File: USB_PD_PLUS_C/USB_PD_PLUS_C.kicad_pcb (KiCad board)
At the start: 4 copper layers, 54 x 45 mm, 57 parts, among them J1 USB3_A, Q2 FS8205A_C908265, U1 NDP1360KC, U10 NDP1360KC, U11 CXP0650-220M-AG(22UH), U12 TPS25740ARGER, U3 CH482D, U4 CXP0650-220M-AG(22UH), U5 LM317L_SOT-89

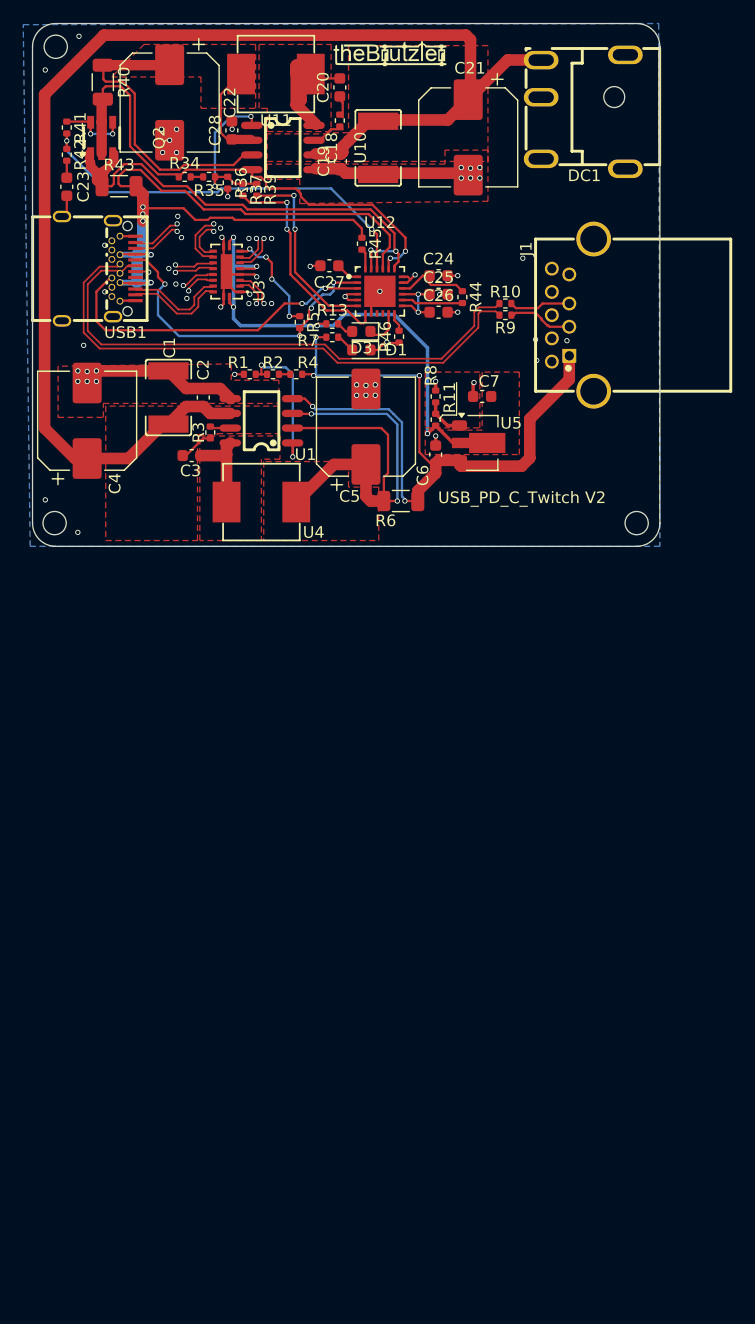
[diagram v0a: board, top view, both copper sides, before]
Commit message: Update Schematic to 3 Port USB-C Power
I updated the schamtic to 3 port usb-C with superspeed and PD working
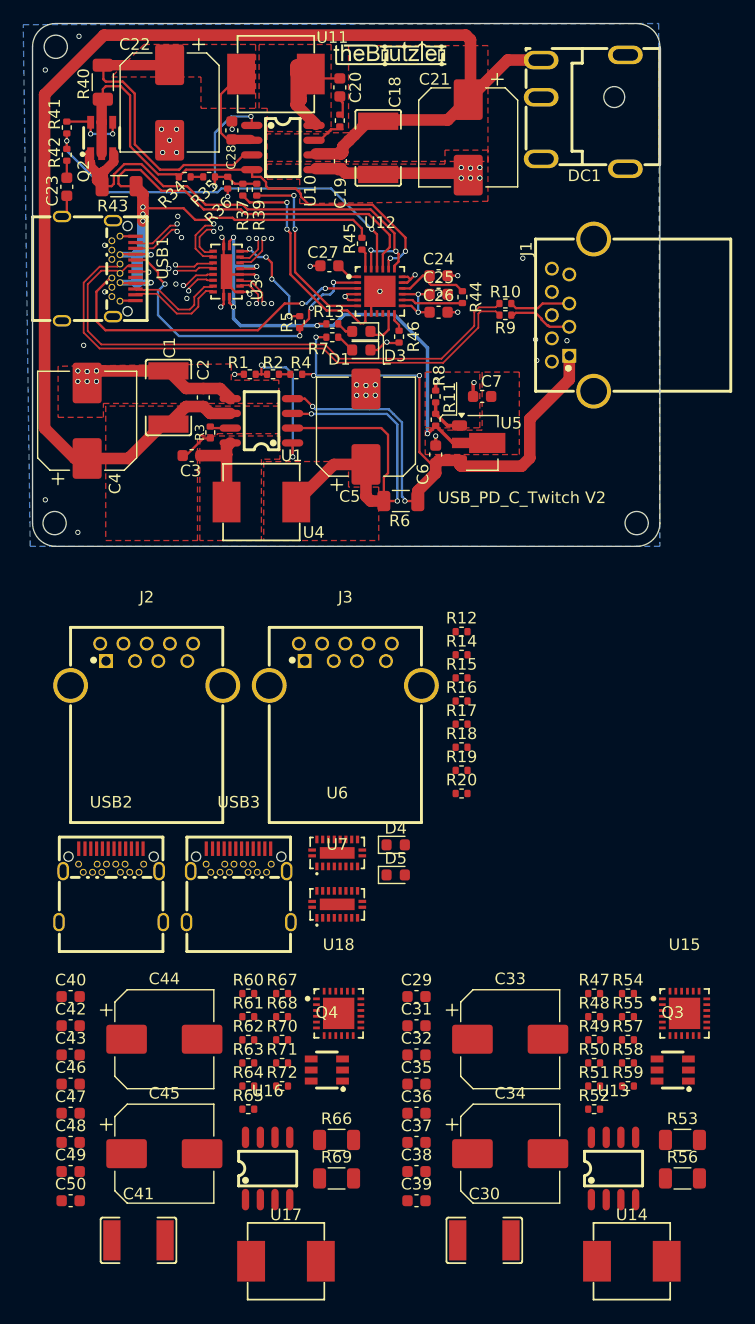
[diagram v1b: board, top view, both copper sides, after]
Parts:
- added C29: 100n, Capacitor_SMD:C_0603_1608Metric, F.Cu at (139.3, 104.7)
- added C30: 22u, easyeda2kicad:C1812, F.Cu at (145.2, 125.6)
- added C31: 100n, Capacitor_SMD:C_0603_1608Metric, F.Cu at (139.3, 107.2)
- added C32: 100n, Capacitor_SMD:C_0603_1608Metric, F.Cu at (139.3, 109.7)
- added C33: 100u, Capacitor_SMD:CP_Elec_8x10, F.Cu at (147.4, 108.3)
- added C34: 100u, Capacitor_SMD:CP_Elec_8x10, F.Cu at (147.4, 118.2)
- added C35: 100n, Capacitor_SMD:C_0603_1608Metric, F.Cu at (139.3, 112.2)
- added C36: 100n, Capacitor_SMD:C_0603_1608Metric, F.Cu at (139.3, 114.7)
- added C37: 100n, Capacitor_SMD:C_0603_1608Metric, F.Cu at (139.3, 117.2)
- added C38: 100n, Capacitor_SMD:C_0603_1608Metric, F.Cu at (139.3, 119.7)
- added C39: 100n, Capacitor_SMD:C_0603_1608Metric, F.Cu at (139.3, 122.2)
- added C40: 100n, Capacitor_SMD:C_0603_1608Metric, F.Cu at (109.6, 104.7)
- added C41: 22u, easyeda2kicad:C1812, F.Cu at (115.4, 125.6)
- added C42: 100n, Capacitor_SMD:C_0603_1608Metric, F.Cu at (109.6, 107.2)
- added C43: 100n, Capacitor_SMD:C_0603_1608Metric, F.Cu at (109.6, 109.7)
- added C44: 100u, Capacitor_SMD:CP_Elec_8x10, F.Cu at (117.6, 108.3)
- added C45: 100u, Capacitor_SMD:CP_Elec_8x10, F.Cu at (117.6, 118.2)
- added C46: 100n, Capacitor_SMD:C_0603_1608Metric, F.Cu at (109.6, 112.2)
- added C47: 100n, Capacitor_SMD:C_0603_1608Metric, F.Cu at (109.6, 114.7)
- added C48: 100n, Capacitor_SMD:C_0603_1608Metric, F.Cu at (109.6, 117.2)
- added C49: 100n, Capacitor_SMD:C_0603_1608Metric, F.Cu at (109.6, 119.7)
- added C50: 100n, Capacitor_SMD:C_0603_1608Metric, F.Cu at (109.6, 122.2)
- added D4: LED, LED_SMD:LED_0603_1608Metric, F.Cu at (137.6, 91.6)
- added D5: LED, LED_SMD:LED_0603_1608Metric, F.Cu at (137.6, 94.2)
- added J2: USB3_A, easyeda2kicad:USB-3.0-A-TH_HC-ST-003-01-Z, F.Cu at (116.1, 76.1)
- added J3: USB3_A, easyeda2kicad:USB-3.0-A-TH_HC-ST-003-01-Z, F.Cu at (133.2, 76.1)
- added Q3: FS8205A_C908265, easyeda2kicad:SOT-23-6_L2.9-W1.6-P0.95-LS2.8-BR, F.Cu at (161.4, 111.0)
- added Q4: FS8205A_C908265, easyeda2kicad:SOT-23-6_L2.9-W1.6-P0.95-LS2.8-BR, F.Cu at (131.6, 111.0)
- added R12: 0R, Resistor_SMD:R_0402_1005Metric, F.Cu at (143.2, 73.2)
- added R14: 10K, Resistor_SMD:R_0402_1005Metric, F.Cu at (143.2, 75.2)
- added R15: 0R, Resistor_SMD:R_0402_1005Metric, F.Cu at (143.2, 77.2)
- added R16: 10K, Resistor_SMD:R_0402_1005Metric, F.Cu at (143.2, 79.2)
- added R17: 22R, Resistor_SMD:R_0402_1005Metric, F.Cu at (143.2, 81.2)
- added R18: 22R, Resistor_SMD:R_0402_1005Metric, F.Cu at (143.2, 83.2)
- added R19: 22R, Resistor_SMD:R_0402_1005Metric, F.Cu at (143.2, 85.2)
- added R20: 22R, Resistor_SMD:R_0402_1005Metric, F.Cu at (143.2, 87.2)
- added R47: 100K, Resistor_SMD:R_0402_1005Metric, F.Cu at (154.6, 104.4)
- added R48: 8K, Resistor_SMD:R_0402_1005Metric, F.Cu at (154.6, 106.4)
- added R49: 25K, Resistor_SMD:R_0402_1005Metric, F.Cu at (154.6, 108.4)
- added R50: 29K, Resistor_SMD:R_0402_1005Metric, F.Cu at (154.6, 110.4)
- added R51: 22R, Resistor_SMD:R_0402_1005Metric, F.Cu at (154.6, 112.4)
- added R52: 18K, Resistor_SMD:R_0402_1005Metric, F.Cu at (154.6, 114.3)
- added R53: 10m, Resistor_SMD:R_1206_3216Metric, F.Cu at (162.2, 117.0)
- added R54: 10K, Resistor_SMD:R_0402_1005Metric, F.Cu at (157.6, 104.4)
- added R55: 10K, Resistor_SMD:R_0402_1005Metric, F.Cu at (157.6, 106.4)
- added R56: 6m, Resistor_SMD:R_1206_3216Metric, F.Cu at (162.2, 120.3)
- added R57: 100K, Resistor_SMD:R_0402_1005Metric, F.Cu at (157.6, 108.4)
- added R58: 100R, Resistor_SMD:R_0402_1005Metric, F.Cu at (157.6, 110.4)
- added R59: 100K, Resistor_SMD:R_0402_1005Metric, F.Cu at (157.6, 112.4)
- added R60: 100K, Resistor_SMD:R_0402_1005Metric, F.Cu at (124.9, 104.4)
- added R61: 8K, Resistor_SMD:R_0402_1005Metric, F.Cu at (124.9, 106.4)
- added R62: 25K, Resistor_SMD:R_0402_1005Metric, F.Cu at (124.9, 108.4)
- added R63: 29K, Resistor_SMD:R_0402_1005Metric, F.Cu at (124.9, 110.4)
- added R64: 22R, Resistor_SMD:R_0402_1005Metric, F.Cu at (124.9, 112.4)
- added R65: 18K, Resistor_SMD:R_0402_1005Metric, F.Cu at (124.9, 114.3)
- added R66: 10m, Resistor_SMD:R_1206_3216Metric, F.Cu at (132.5, 117.0)
- added R67: 10K, Resistor_SMD:R_0402_1005Metric, F.Cu at (127.8, 104.4)
- added R68: 10K, Resistor_SMD:R_0402_1005Metric, F.Cu at (127.8, 106.4)
- added R69: 6m, Resistor_SMD:R_1206_3216Metric, F.Cu at (132.5, 120.3)
- added R70: 100K, Resistor_SMD:R_0402_1005Metric, F.Cu at (127.8, 108.4)
- added R71: 100R, Resistor_SMD:R_0402_1005Metric, F.Cu at (127.8, 110.4)
- added R72: 100K, Resistor_SMD:R_0402_1005Metric, F.Cu at (127.8, 112.4)
- added U13: NDP1360KC, easyeda2kicad:SOP-8_L4.9-W3.9-P1.27-LS6.0-BL, F.Cu at (156.3, 119.5)
- added U14: CXP0650-220M-AG(22UH), easyeda2kicad:IND-SMD_L7.1-W6.6_CXP0650, F.Cu at (157.9, 127.4)
- added U15: TPS25740ARGER, easyeda2kicad:VQFN-24_L4.0-W4.0-P0.50-TL-EP, F.Cu at (162.4, 106.1)
- added U16: NDP1360KC, easyeda2kicad:SOP-8_L4.9-W3.9-P1.27-LS6.0-BL, F.Cu at (126.5, 119.5)
- added U17: CXP0650-220M-AG(22UH), easyeda2kicad:IND-SMD_L7.1-W6.6_CXP0650, F.Cu at (128.1, 127.4)
- added U18: TPS25740ARGER, easyeda2kicad:VQFN-24_L4.0-W4.0-P0.50-TL-EP, F.Cu at (132.7, 106.1)
- added U6: CH482D, easyeda2kicad:VFQFN-20_L4.5-W2.5-P0.5-BL-EP, F.Cu at (132.5, 92.3)
- added U7: CH482D, easyeda2kicad:VFQFN-20_L4.5-W2.5-P0.5-BL-EP, F.Cu at (132.5, 96.7)
- added USB2: HX TYPE-C 24P QCHT, easyeda2kicad:TYPE-C-SMD_TYPE-C-24P-QCHT, F.Cu at (113.1, 95.1)
- added USB3: HX TYPE-C 24P QCHT, easyeda2kicad:TYPE-C-SMD_TYPE-C-24P-QCHT, F.Cu at (124.0, 95.1)

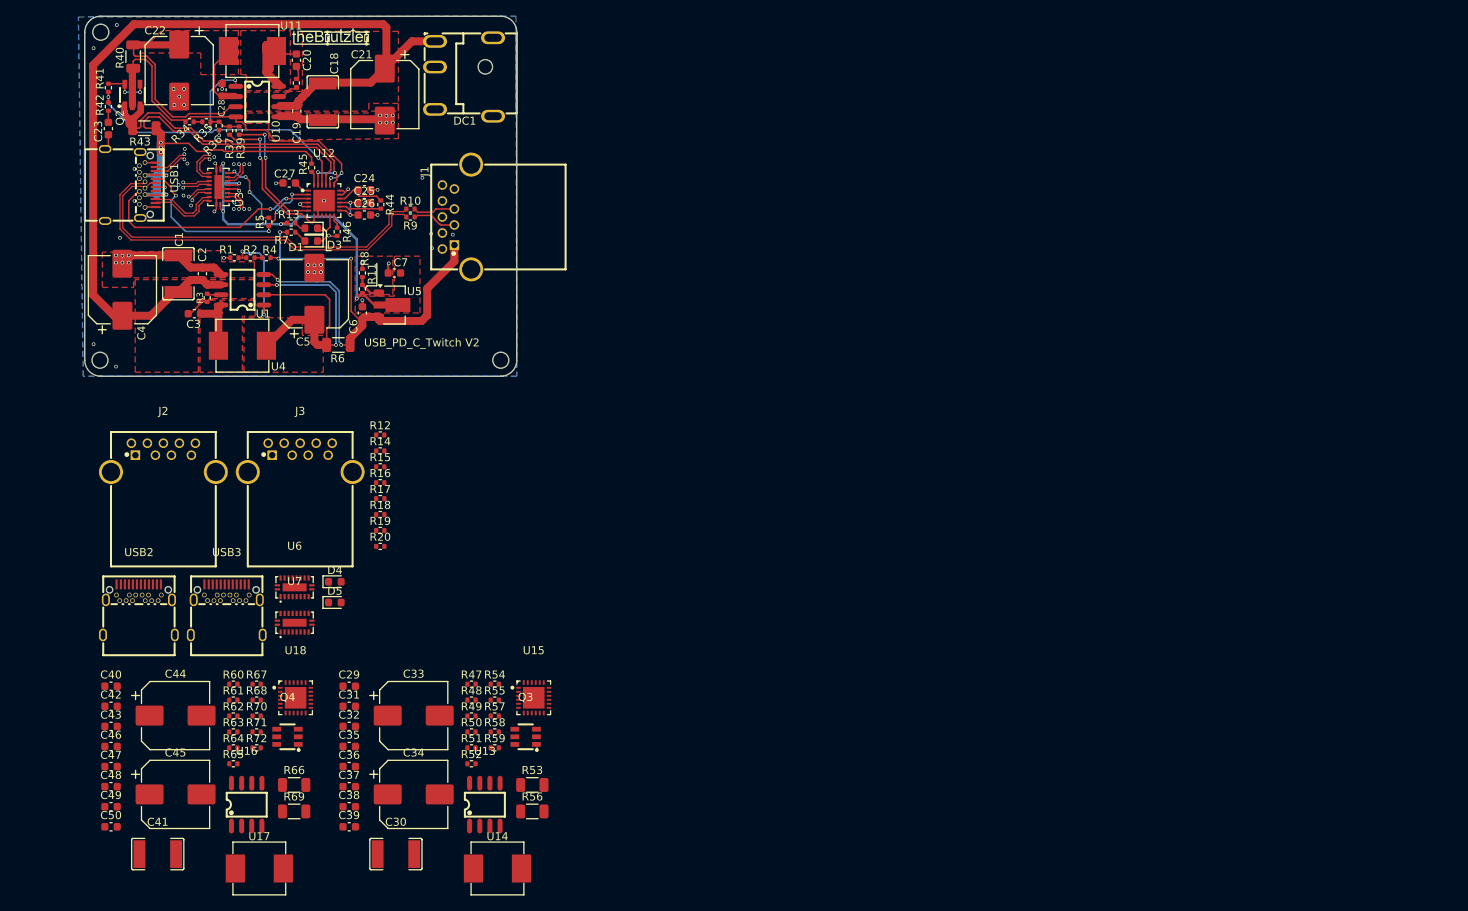
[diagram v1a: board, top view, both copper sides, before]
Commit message: update USB PD PCB to 3 in 3 out
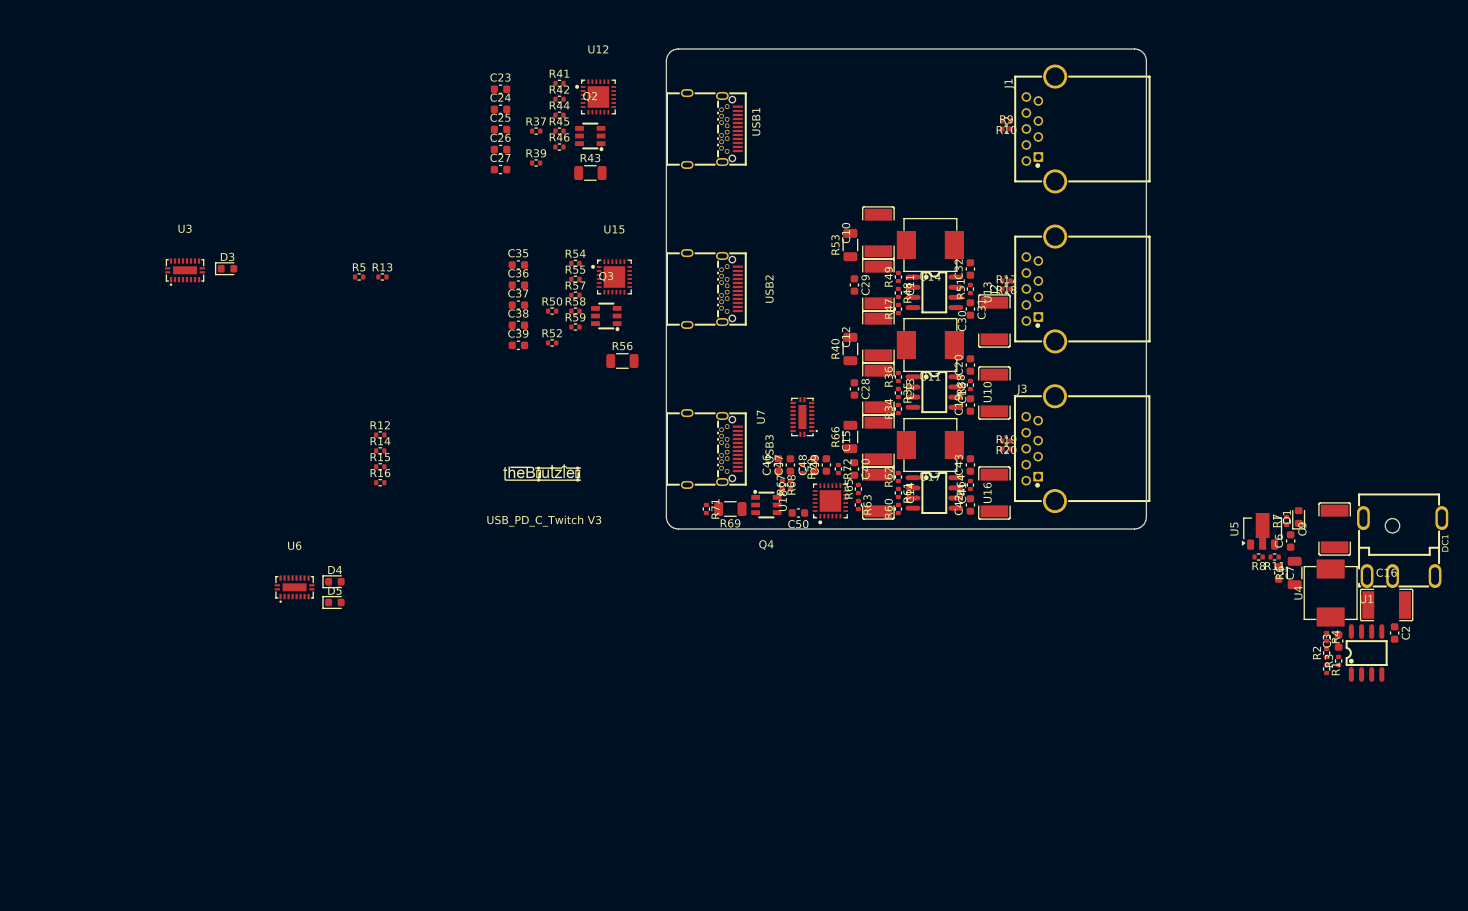
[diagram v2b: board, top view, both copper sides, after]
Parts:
- removed C1: 2u2, easyeda2kicad:C1812
- removed C21, C22, C33, C34, C4, C44, C45, C5: 100u, Capacitor_SMD:CP_Elec_8x10
- added C10: 22u, easyeda2kicad:C1812, F.Cu at (205.5, 48.0)
- added C11: 22u, easyeda2kicad:C1812, F.Cu at (205.5, 54.5)
- added C12: 22u, easyeda2kicad:C1812, F.Cu at (205.5, 61.0)
- added C13: 22u, easyeda2kicad:C1812, F.Cu at (205.5, 67.5)
- added C14: 22u, easyeda2kicad:C1812, F.Cu at (205.5, 80.5)
- added C15: 22u, easyeda2kicad:C1812, F.Cu at (205.5, 74.0)
- added C16: 22u, easyeda2kicad:C1812, F.Cu at (269.0, 94.5)
- added C9: 22u, easyeda2kicad:C1812, F.Cu at (262.5, 85.0)
- moved C2 155.6 mm to (270.0, 98.0)
- moved C3 148.8 mm to (263.0, 99.0), turned to 90 degrees
- moved R3 148.5 mm to (263.0, 101.5), turned to 90 degrees
- moved U1 147.7 mm to (266.5, 100.5), turned to 0 degrees
- moved R1 145.9 mm to (261.5, 102.5), turned to -90 degrees
- moved R2 143.3 mm to (261.5, 100.5), turned to 90 degrees
- moved R4 140.8 mm to (261.5, 98.5), turned to -90 degrees
- moved U4 139.5 mm to (262.0, 93.0), turned to 90 degrees
- moved DC1 131.2 mm to (271.0, 87.3), turned to -90 degrees
- moved R7 129.6 mm to (256.5, 84.0), turned to 90 degrees
- moved D1 128.2 mm to (258.0, 83.5), turned to 90 degrees
- moved R6 122.9 mm to (257.5, 90.5), turned to 90 degrees
- moved C6 119.5 mm to (257.0, 86.5)
- moved R11 118.8 mm to (255.0, 88.5), turned to 180 degrees
- moved R8 117.5 mm to (253.0, 88.5), turned to 180 degrees
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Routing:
- net +24V: track 114.8 -> 0.00 mm
- net /A_VBUS: track 72.9 -> 0.00 mm, vias 5 -> 0
- net +5V: track 64.2 -> 0.00 mm, vias 5 -> 0
- net GND: track 62.4 -> 0.00 mm, vias 62 -> 0
- net /A_D-: track 51.5 -> 0.00 mm, vias 1 -> 0
- net /A_D+: track 48.1 -> 0.00 mm
- net Net-(U10-CSN2): track 44.6 -> 0.00 mm, vias 2 -> 0
- net +3V3: track 43.5 -> 0.00 mm, vias 5 -> 0
- net Net-(U1-CSN1): track 43.3 -> 0.00 mm, vias 2 -> 0
- net Net-(Q2-S1): track 42.7 -> 0.00 mm, vias 2 -> 0
- net Net-(U12-GDNG): track 35.1 -> 0.00 mm, vias 2 -> 0
- net Net-(U10-CSN1): track 34.4 -> 0.00 mm
- net /A_SSRX-: track 31.8 -> 0.00 mm, vias 1 -> 0
- net /A_SSRX+: track 31.8 -> 0.00 mm, vias 1 -> 0
- net /A_SSTX+: track 30.6 -> 0.00 mm, vias 1 -> 0
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- removed copper zone on F.Cu, net +24V
- removed copper zone on F.Cu, net +3V3
- removed copper zone on B.Cu, net GND
- removed copper zone on F.Cu, net GND
- removed copper zone on In1.Cu, net GND
- removed copper zone on In2.Cu, net GND
- removed copper zone on F.Cu, net Net-(U1-CSN1)
- removed copper zone on F.Cu, net Net-(U1-SW)
- removed copper zone on F.Cu, net Net-(U10-CSN1)
- removed copper zone on F.Cu, net Net-(U10-SW)
- removed copper zone on F.Cu, net Net-(U5-ADJ)
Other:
- board size 54 x 45 mm -> 60 x 60 mm
- board text added: "R1"
- board text added: "R14"
- board text added: "R2"
- board text added: "USB_PD_C_Twitch V3"
- board text removed: "USB_PD_C_Twitch V2"
